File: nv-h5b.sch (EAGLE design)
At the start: 17 parts, among them IC1 TINY13A-20SSU, J1 22-05-7038-03

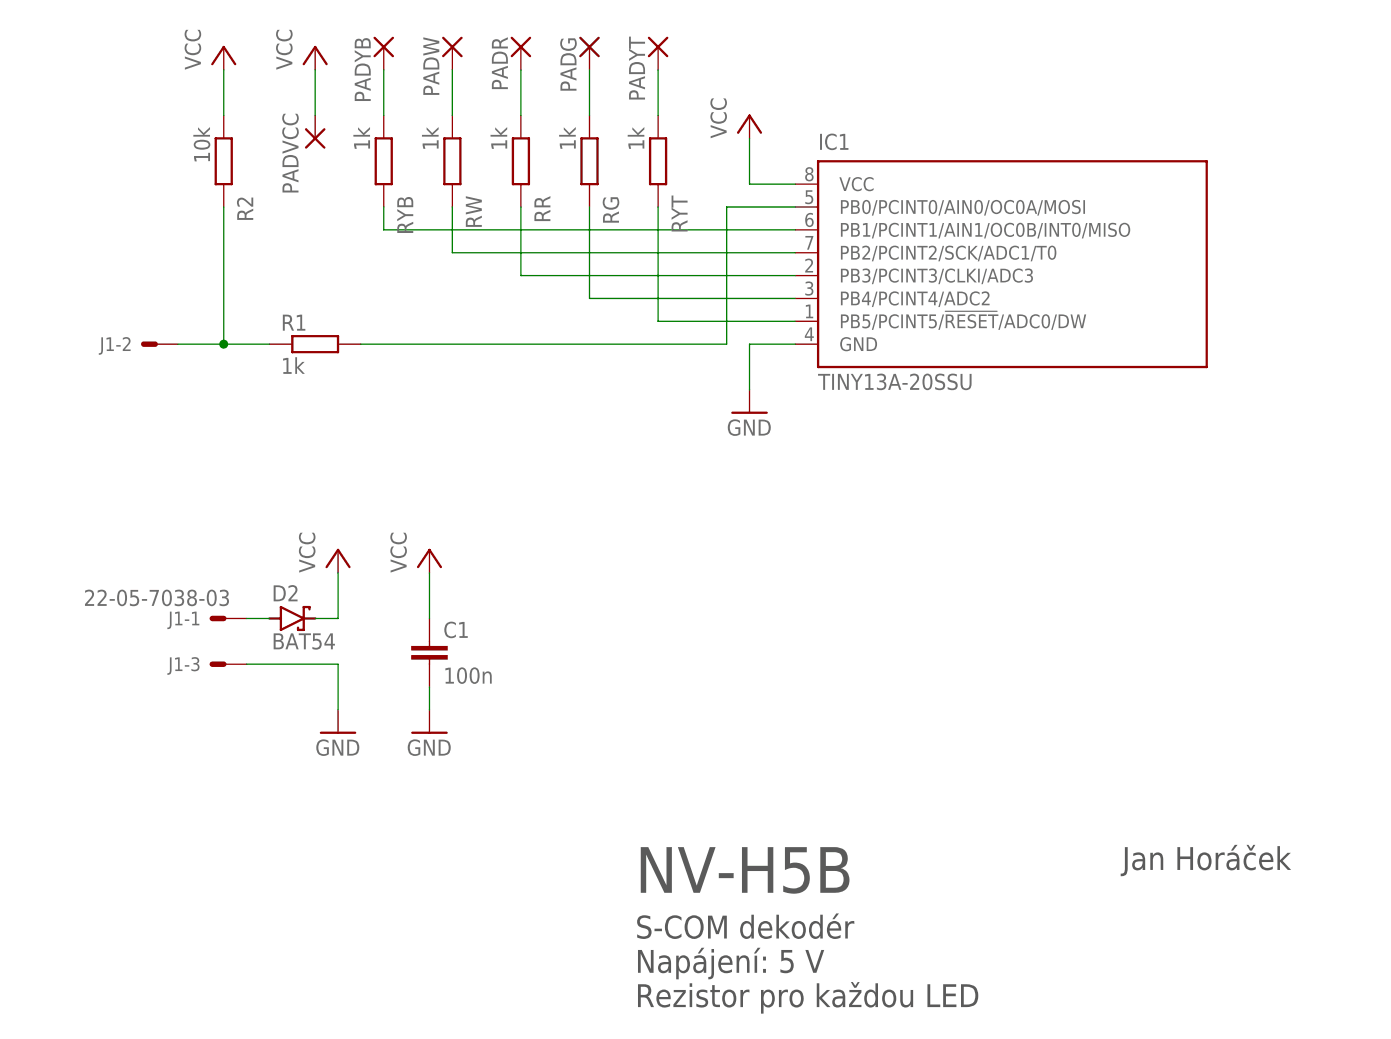
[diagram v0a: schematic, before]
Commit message: Increase LED resistors (~ max. 3 mA/ LED).
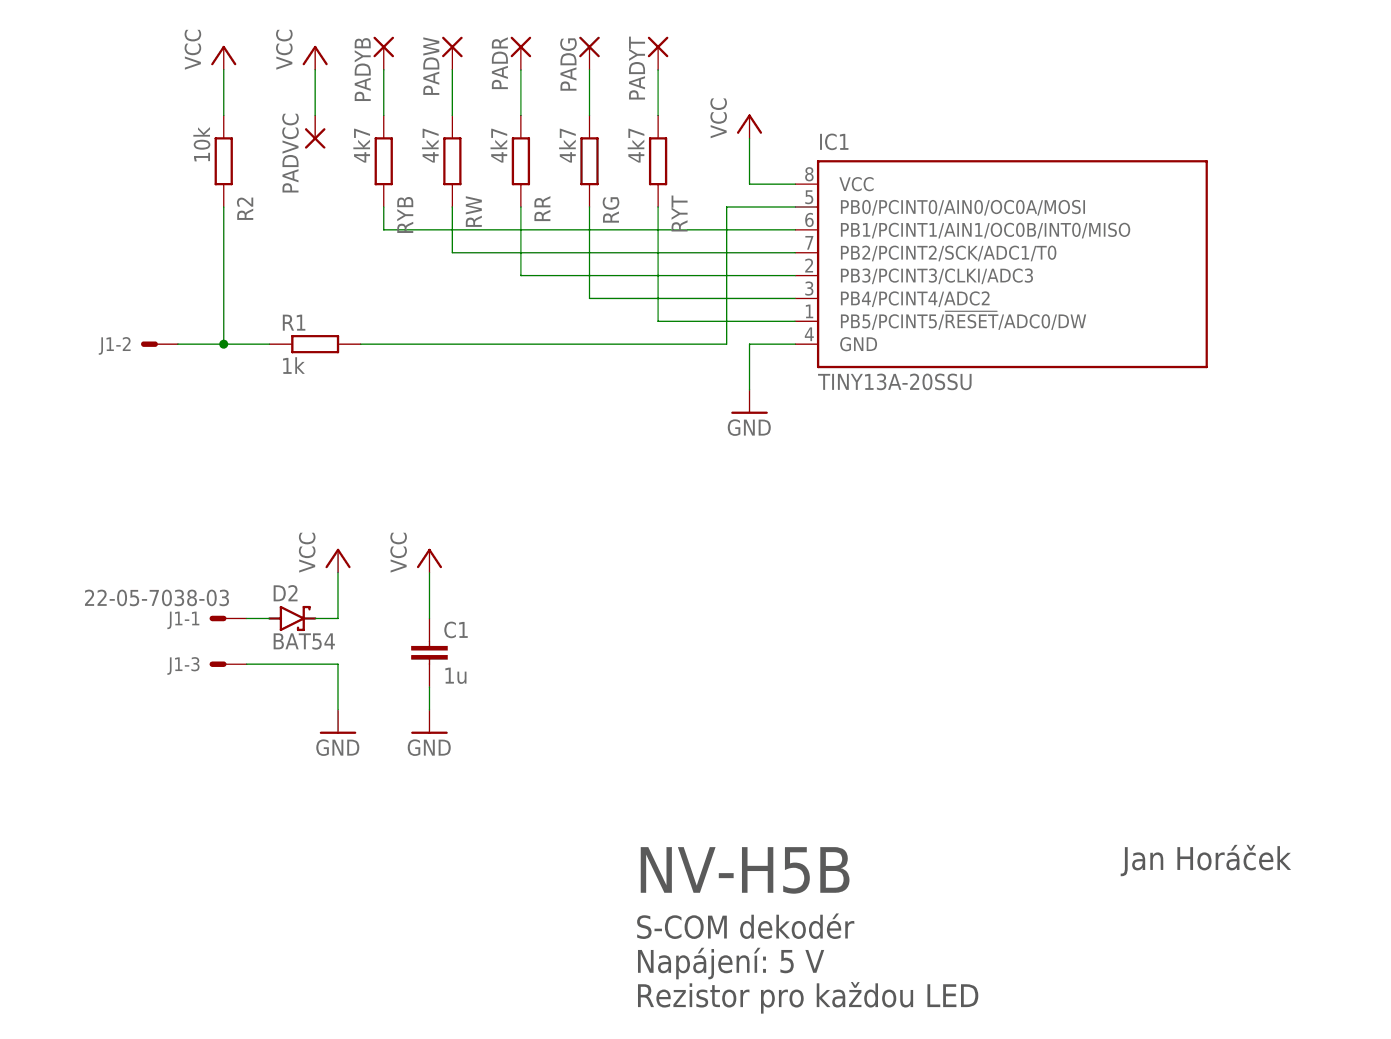
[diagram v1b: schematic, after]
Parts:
- C1: value 100n -> 1u
- RG, RR, RW, RYB, RYT: value 1k -> 4k7
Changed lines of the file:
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@@
 <part name="P+1" library="supply1" library_urn="urn:adsk.eagle:library:371" deviceset="VCC" device=""/>
 <part name="GND1" library="supply1" library_urn="urn:adsk.eagle:library:371" deviceset="GND" device=""/>
-<part name="C1" library="rcl" deviceset="C-EU" device="C0805" value="100n"/>
+<part name="C1" library="rcl" deviceset="C-EU" device="C0805" value="1u"/>
 <part name="P+2" library="supply1" library_urn="urn:adsk.eagle:library:371" deviceset="VCC" device=""/>
 <part name="GND2" library="supply1" library_urn="urn:adsk.eagle:library:371" deviceset="GND" device=""/>
-<part name="RR" library="rcl" deviceset="R-EU_" device="R0805" value="1k"/>
-<part name="RG" library="rcl" deviceset="R-EU_" device="R0805" value="1k"/>
-<part name="RYT" library="rcl" deviceset="R-EU_" device="R0805" value="1k"/>
-<part name="RYB" library="rcl" deviceset="R-EU_" device="R0805" value="1k"/>
-<part name="RW" library="rcl" deviceset="R-EU_" device="R0805" value="1k"/>
+<part name="RR" library="rcl" deviceset="R-EU_" device="R0805" value="4k7"/>
+<part name="RG" library="rcl" deviceset="R-EU_" device="R0805" value="4k7"/>
+<part name="RYT" library="rcl" deviceset="R-EU_" device="R0805" value="4k7"/>
+<part name="RYB" library="rcl" deviceset="R-EU_" device="R0805" value="4k7"/>
+<part name="RW" library="rcl" deviceset="R-EU_" device="R0805" value="4k7"/>
 <part name="PADR" library="wirepad" deviceset="SMD3" device=""/>
 <part name="PADG" library="wirepad" deviceset="SMD3" device=""/>

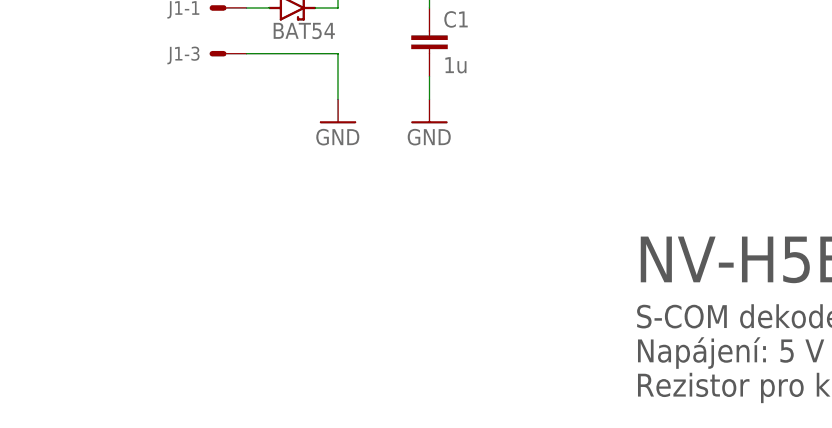
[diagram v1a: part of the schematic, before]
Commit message: Add info about power consumption.
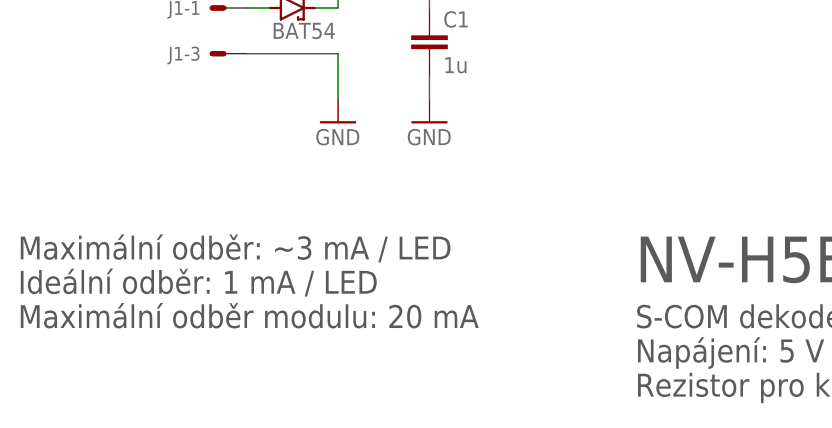
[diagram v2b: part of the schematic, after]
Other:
- note added: "Maximální odběr: ~3 mA / LED Ideální odběr: 1 mA / LED Maximální odběr modulu: 20 mA"
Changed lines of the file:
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@@
 Napájení: 5 V
 Rezistor pro každou LED</text>
+<text x="17.78" y="12.7" size="2.54" layer="97">Maximální odběr: ~3 mA / LED
+Ideální odběr: 1 mA / LED
+Maximální odběr modulu: 20 mA</text>
 </plain>
 <instances>
